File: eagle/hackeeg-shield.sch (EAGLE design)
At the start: 140 parts, among them IC1 ADS1299IPAG, IC10 TXB0108PWR, IC11 TXB0108PWR, IC2 TPS72325DBVT, IC3 TPS73225DBVT, IC5 24AA256UID, IC6 TPS60403DBVT, IC7 OPA376DBV, IC8 OPA376DBV, IC9 TXS0102DCUR

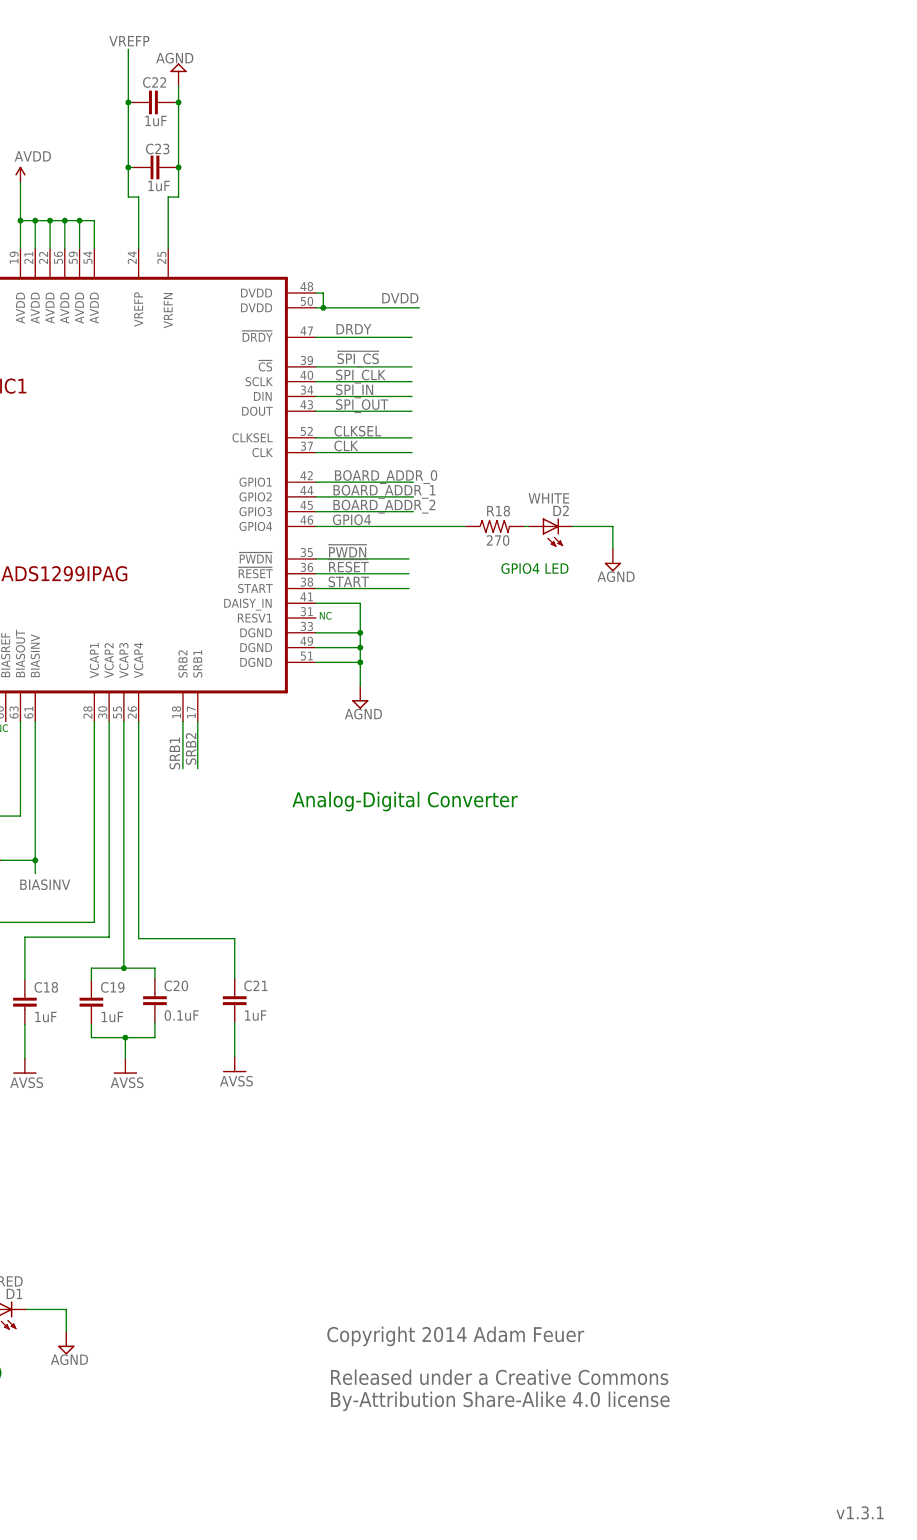
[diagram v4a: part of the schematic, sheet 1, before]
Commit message: fix for bipolar mode 2.25x problem (VREFN-AVSS)
- disconnected VREFN from AGND
- connected VREFN to AVSS
- rerouted traces
- minor labeling changes - labeled all board to board connectors
- bumped version to 1.4.0
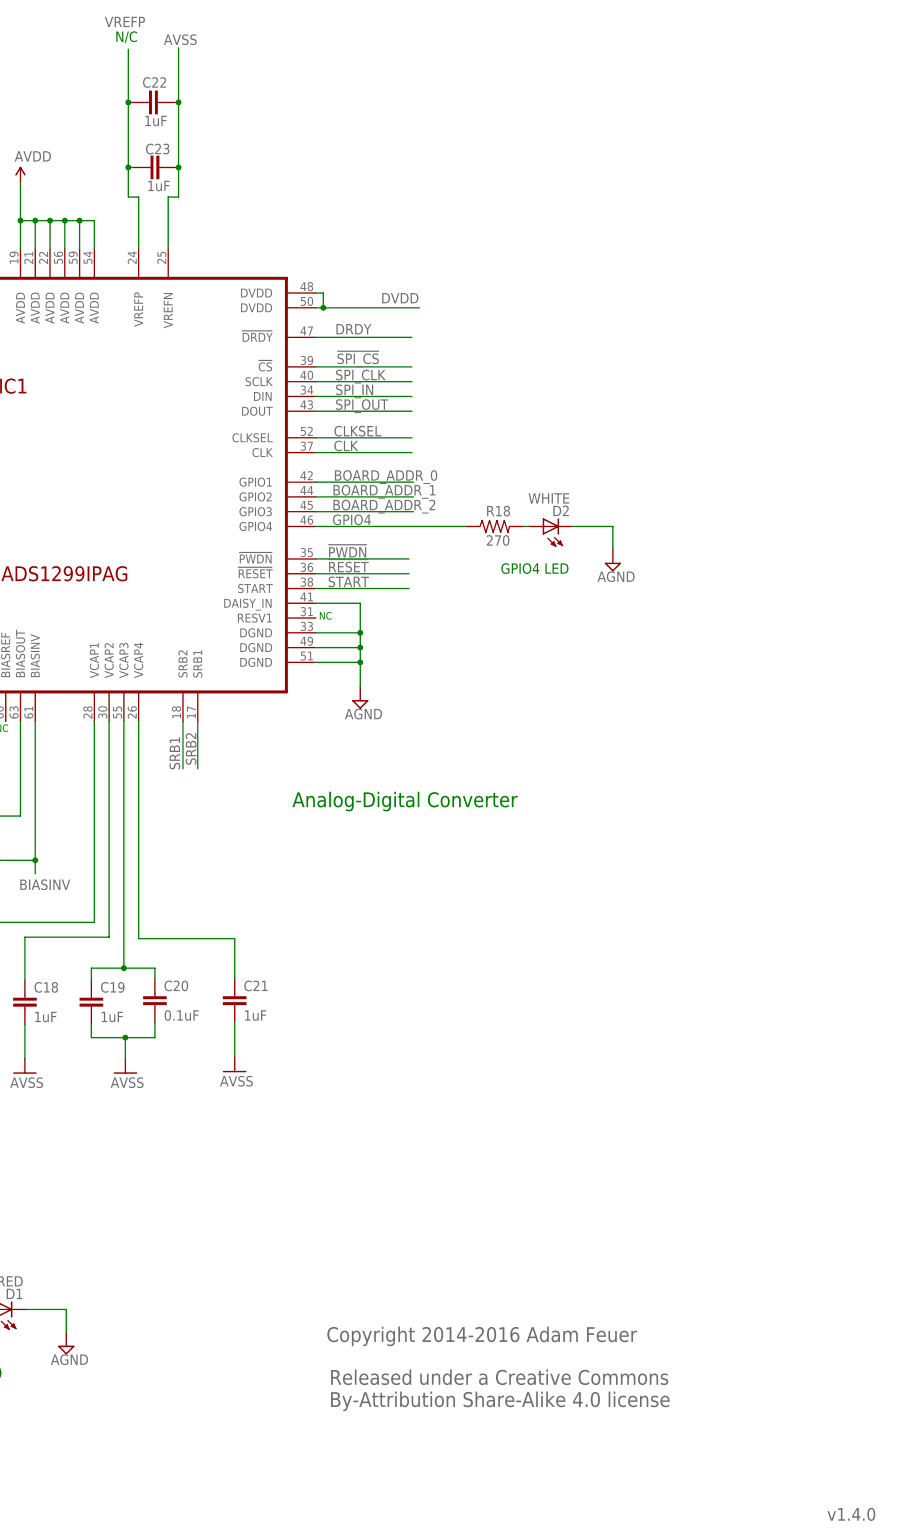
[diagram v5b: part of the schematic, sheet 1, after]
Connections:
- net AGND: no longer C22.2, C23.2, IC1.VREFN
- net AVSS: now also C22.2, C23.2, IC1.VREFN
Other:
- note added: "Copyright 2014-2016 Adam Feuer"
- note added: "N/C"
- note added: "v1.4.0"
- note removed: "Copyright 2014 Adam Feuer"
- note removed: "v1.3.1"
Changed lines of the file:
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@@
 <setting verticaltext="up"/>
 </settings>
-<grid distance="0.1" unitdist="inch" unit="inch" style="lines" multiple="1" display="no" altdistance="0.01" altunitdist="inch" altunit="inch"/>
+<grid distance="0.01" unitdist="inch" unit="inch" style="lines" multiple="1" display="no" altdistance="0.001" altunitdist="inch" altunit="inch"/>
 <layers>
 <layer number="1" name="Top" color="4" fill="1" visible="no" active="no"/>
@@
 <part name="SUPPLY10" library="supply2" deviceset="AGND" device=""/>
 <part name="SUPPLY15" library="supply2" deviceset="AGND" device=""/>
-<part name="SUPPLY20" library="supply2" deviceset="AGND" device=""/>
 <part name="AVSS1" library="SparkFun-Aesthetics" deviceset="GND" device="" value="AVSS"/>
 <part name="AVSS2" library="SparkFun-Aesthetics" deviceset="GND" device="" value="AVSS"/>
@@
 <text x="329.184" y="26.416" size="2.54" layer="95">Released under a Creative Commons
 By-Attribution Share-Alike 4.0 license</text>
-<text x="328.676" y="37.592" size="2.54" layer="95">Copyright 2014 Adam Feuer</text>
-<text x="416.306" y="7.112" size="2.1844" layer="95">v1.3.1</text>
+<text x="328.676" y="37.592" size="2.54" layer="95">Copyright 2014-2016 Adam Feuer</text>
+<text x="414.782" y="6.858" size="2.1844" layer="95">v1.4.0</text>
 <text x="246.634" y="212.344" size="1.778" layer="91">NC</text>
 <text x="327.406" y="161.798" size="1.27" layer="91">NC</text>
@@
 <text x="256.286" y="30.988" size="2.54" layer="91">Power LED</text>
 <text x="271.78" y="142.494" size="1.27" layer="91">NC</text>
+<text x="292.354" y="261.112" size="1.778" layer="91">N/C</text>
 </plain>
 <instances>
@@
 <instance part="SUPPLY10" gate="G$1" x="81.28" y="187.96"/>
 <instance part="SUPPLY15" gate="G$1" x="48.26" y="189.484"/>
-<instance part="SUPPLY20" gate="G$1" x="303.276" y="256.032" rot="R180"/>
 <instance part="AVSS1" gate="1" x="49.276" y="233.68" smashed="yes">
 <attribute name="VALUE" x="46.736" y="231.14" size="1.778" layer="96"/>
@@
 <wire x1="295.402" y1="239.522" x2="294.64" y2="239.522" width="0.1524" layer="91"/>
 <wire x1="294.64" y1="250.698" x2="294.64" y2="259.842" width="0.1524" layer="91"/>
-<label x="291.338" y="260.35" size="1.778" layer="95"/>
+<label x="290.576" y="263.652" size="1.778" layer="95"/>
 <pinref part="C23" gate="G$1" pin="1"/>
 <junction x="294.64" y="239.522"/>
@@
 <wire x1="48.26" y1="192.024" x2="48.26" y2="196.596" width="0.1524" layer="91"/>
 <pinref part="SUPPLY15" gate="G$1" pin="AGND"/>
-</segment>
-<segment>
-<wire x1="301.498" y1="225.552" x2="301.498" y2="234.442" width="0.1524" layer="91"/>
-<wire x1="301.498" y1="234.442" x2="303.276" y2="234.442" width="0.1524" layer="91"/>
-<wire x1="303.276" y1="234.442" x2="303.276" y2="239.522" width="0.1524" layer="91"/>
-<wire x1="303.276" y1="239.522" x2="303.276" y2="250.698" width="0.1524" layer="91"/>
-<wire x1="303.276" y1="250.698" x2="303.276" y2="253.492" width="0.1524" layer="91"/>
-<junction x="303.276" y="250.698"/>
-<pinref part="C23" gate="G$1" pin="2"/>
-<wire x1="303.022" y1="239.522" x2="303.276" y2="239.522" width="0.1524" layer="91"/>
-<junction x="303.276" y="239.522"/>
-<pinref part="C22" gate="G$1" pin="2"/>
-<wire x1="303.276" y1="250.698" x2="302.768" y2="250.698" width="0.1524" layer="91"/>
-<pinref part="SUPPLY20" gate="G$1" pin="AGND"/>
-<pinref part="IC1" gate="G$1" pin="VREFN"/>
 </segment>
 <segment>
@@
 <wire x1="312.928" y1="92.456" x2="312.928" y2="86.614" width="0.1524" layer="91"/>
 </segment>
+<segment>
+<wire x1="301.498" y1="225.552" x2="301.498" y2="234.442" width="0.1524" layer="91"/>
+<wire x1="301.498" y1="234.442" x2="303.276" y2="234.442" width="0.1524" layer="91"/>
+<wire x1="303.276" y1="234.442" x2="303.276" y2="239.522" width="0.1524" layer="91"/>
+<wire x1="303.276" y1="239.522" x2="303.276" y2="250.698" width="0.1524" layer="91"/>
+<wire x1="303.276" y1="250.698" x2="303.276" y2="260.096" width="0.1524" layer="91"/>
+<junction x="303.276" y="250.698"/>
+<pinref part="C23" gate="G$1" pin="2"/>
+<wire x1="303.022" y1="239.522" x2="303.276" y2="239.522" width="0.1524" layer="91"/>
+<junction x="303.276" y="239.522"/>
+<pinref part="C22" gate="G$1" pin="2"/>
+<wire x1="303.276" y1="250.698" x2="302.768" y2="250.698" width="0.1524" layer="91"/>
+<pinref part="IC1" gate="G$1" pin="VREFN"/>
+<label x="300.736" y="260.604" size="1.778" layer="95"/>
+</segment>
 </net>
 <net name="BIASINV" class="0">
@@
 <text x="320.802" y="26.416" size="2.54" layer="95">Released under a Creative Commons
 By-Attribution Share-Alike 4.0 license</text>
-<text x="320.294" y="37.592" size="2.54" layer="95">Copyright 2014 Adam Feuer</text>
+<text x="320.294" y="37.592" size="2.54" layer="95">Copyright 2014-2016 Adam Feuer</text>
 <text x="65.532" y="264.668" size="2.54" layer="91">Input Filtering</text>
 <text x="160.274" y="254.762" size="2.54" layer="91">(This side to ADS1299 inputs)</text>
@@
 <text x="326.136" y="26.416" size="2.54" layer="95">Released under a Creative Commons
 By-Attribution Share-Alike 4.0 license</text>
-<text x="325.628" y="37.592" size="2.54" layer="95">Copyright 2014 Adam Feuer</text>
+<text x="325.628" y="37.592" size="2.54" layer="95">Copyright 2014-2016 Adam Feuer</text>
 <text x="315.468" y="84.582" size="2.54" layer="91">Shield Connectors</text>
 <text x="356.616" y="254" size="1.524" layer="91">SCL1</text>

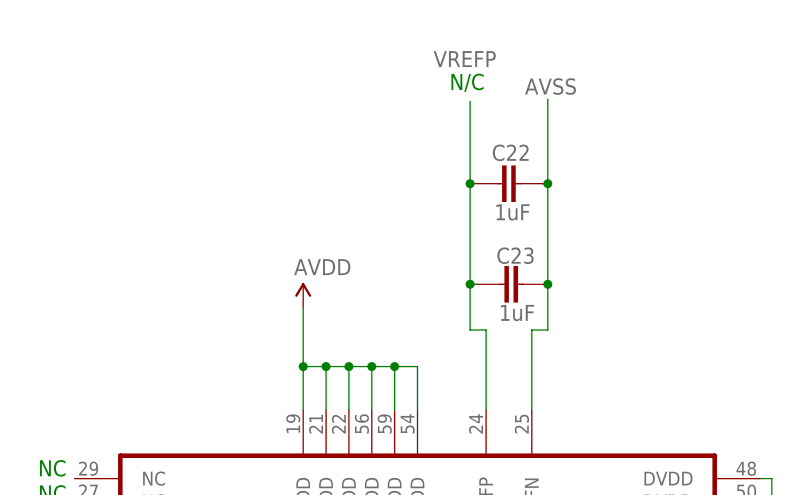
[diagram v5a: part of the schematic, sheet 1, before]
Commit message: changed C22 to 10uF; C23 to 0.1uF
- to match eval board schematic
- and added VREFP test point
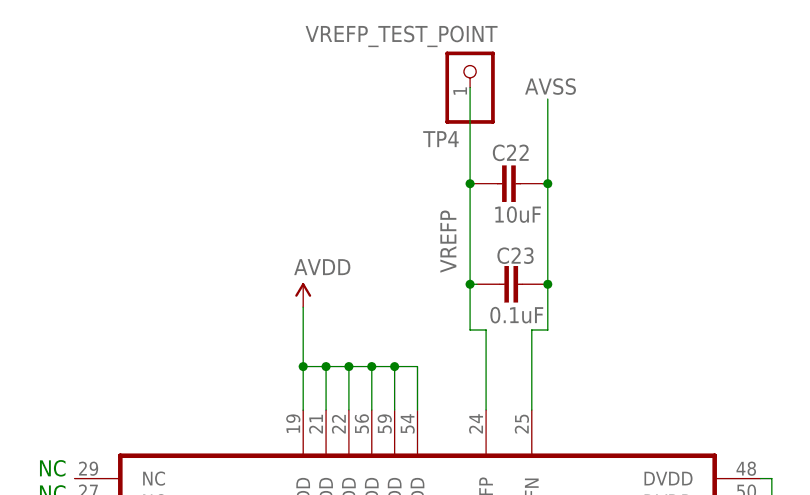
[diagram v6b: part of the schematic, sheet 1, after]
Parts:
- added TP4: VREFP_TEST_POINT, adafruit:PINHD-1X1
- C22: value 1uF -> 10uF
- C23: value 1uF -> 0.1uF
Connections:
- net VREFP: now also TP4.1
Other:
- note removed: "N/C"
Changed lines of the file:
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@@
 <setting verticaltext="up"/>
 </settings>
-<grid distance="0.01" unitdist="inch" unit="inch" style="lines" multiple="1" display="no" altdistance="0.001" altunitdist="inch" altunit="inch"/>
+<grid distance="0.1" unitdist="inch" unit="inch" style="lines" multiple="1" display="no" altdistance="0.01" altunitdist="inch" altunit="inch"/>
 <layers>
-<layer number="1" name="Top" color="4" fill="1" visible="no" active="no"/>
-<layer number="2" name="Route2" color="1" fill="3" visible="no" active="no"/>
-<layer number="3" name="Route3" color="4" fill="3" visible="no" active="no"/>
-<layer number="14" name="Route14" color="1" fill="6" visible="no" active="no"/>
-<layer number="15" name="Route15" color="4" fill="6" visible="no" active="no"/>
-<layer number="16" name="Bottom" color="1" fill="1" visible="no" active="no"/>
-<layer number="17" name="Pads" color="2" fill="1" visible="no" active="no"/>
-<layer number="18" name="Vias" color="2" fill="1" visible="no" active="no"/>
-<layer number="19" name="Unrouted" color="6" fill="1" visible="no" active="no"/>
-<layer number="20" name="Dimension" color="15" fill="1" visible="no" active="no"/>
-<layer number="21" name="tPlace" color="7" fill="1" visible="no" active="no"/>
-<layer number="22" name="bPlace" color="7" fill="1" visible="no" active="no"/>
-<layer number="23" name="tOrigins" color="15" fill="1" visible="no" active="no"/>
-<layer number="24" name="bOrigins" color="15" fill="1" visible="no" active="no"/>
-<layer number="25" name="tNames" color="7" fill="1" visible="no" active="no"/>
-<layer number="26" name="bNames" color="7" fill="1" visible="no" active="no"/>
-<layer number="27" name="tValues" color="7" fill="1" visible="no" active="no"/>
-<layer number="28" name="bValues" color="7" fill="1" visible="no" active="no"/>
+<layer number="1" name="Top" color="4" fill="1" visible="yes" active="no"/>
+<layer number="2" name="Route2" color="3" fill="1" visible="yes" active="no"/>
+<layer number="3" name="Route3" color="4" fill="3" visible="yes" active="no"/>
+<layer number="14" name="Route14" color="1" fill="6" visible="yes" active="no"/>
+<layer number="15" name="Route15" color="15" fill="1" visible="yes" active="no"/>
+<layer number="16" name="Bottom" color="1" fill="1" visible="yes" active="no"/>
+<layer number="17" name="Pads" color="2" fill="1" visible="yes" active="no"/>
+<layer number="18" name="Vias" color="2" fill="1" visible="yes" active="no"/>
+<layer number="19" name="Unrouted" color="14" fill="1" visible="yes" active="no"/>
+<layer number="20" name="Dimension" color="15" fill="1" visible="yes" active="no"/>
+<layer number="21" name="tPlace" color="7" fill="1" visible="yes" active="no"/>
+<layer number="22" name="bPlace" color="7" fill="1" visible="yes" active="no"/>
+<layer number="23" name="tOrigins" color="15" fill="1" visible="yes" active="no"/>
+<layer number="24" name="bOrigins" color="15" fill="1" visible="yes" active="no"/>
+<layer number="25" name="tNames" color="7" fill="1" visible="yes" active="no"/>
+<layer number="26" name="bNames" color="7" fill="1" visible="yes" active="no"/>
+<layer number="27" name="tValues" color="7" fill="1" visible="yes" active="no"/>
+<layer number="28" name="bValues" color="7" fill="1" visible="yes" active="no"/>
 <layer number="29" name="tStop" color="3" fill="9" visible="no" active="no"/>
 <layer number="30" name="bStop" color="7" fill="6" visible="no" active="no"/>
@@
 <layer number="35" name="tGlue" color="7" fill="4" visible="no" active="no"/>
 <layer number="36" name="bGlue" color="7" fill="5" visible="no" active="no"/>
-<layer number="37" name="tTest" color="7" fill="1" visible="no" active="no"/>
-<layer number="38" name="bTest" color="7" fill="1" visible="no" active="no"/>
+<layer number="37" name="tTest" color="7" fill="1" visible="yes" active="no"/>
+<layer number="38" name="bTest" color="7" fill="1" visible="yes" active="no"/>
 <layer number="39" name="tKeepout" color="13" fill="1" visible="no" active="no"/>
 <layer number="40" name="bKeepout" color="5" fill="1" visible="no" active="no"/>
@@
 <layer number="44" name="Drills" color="7" fill="1" visible="no" active="no"/>
 <layer number="45" name="Holes" color="7" fill="1" visible="no" active="no"/>
-<layer number="46" name="Milling" color="3" fill="1" visible="no" active="no"/>
-<layer number="47" name="Measures" color="7" fill="1" visible="no" active="no"/>
-<layer number="48" name="Document" color="7" fill="1" visible="no" active="no"/>
-<layer number="49" name="Reference" color="7" fill="1" visible="no" active="no"/>
-<layer number="50" name="dxf" color="7" fill="1" visible="no" active="no"/>
-<layer number="51" name="tDocu" color="6" fill="1" visible="no" active="no"/>
-<layer number="52" name="bDocu" color="6" fill="1" visible="no" active="no"/>
-<layer number="53" name="tGND_GNDA" color="7" fill="9" visible="no" active="no"/>
-<layer number="54" name="bGND_GNDA" color="1" fill="9" visible="no" active="no"/>
-<layer number="56" name="wert" color="7" fill="1" visible="no" active="no"/>
-<layer number="57" name="tCAD" color="7" fill="1" visible="no" active="no"/>
+<layer number="46" name="Milling" color="3" fill="1" visible="yes" active="no"/>
+<layer number="47" name="Measures" color="7" fill="1" visible="yes" active="no"/>
+<layer number="48" name="Document" color="7" fill="1" visible="yes" active="no"/>
+<layer number="49" name="Reference" color="7" fill="1" visible="yes" active="no"/>
+<layer number="50" name="dxf" color="7" fill="1" visible="yes" active="no"/>
+<layer number="51" name="tDocu" color="6" fill="1" visible="yes" active="no"/>
+<layer number="52" name="bDocu" color="6" fill="1" visible="yes" active="no"/>
+<layer number="53" name="tGND_GNDA" color="7" fill="9" visible="yes" active="no"/>
+<layer number="54" name="bGND_GNDA" color="1" fill="9" visible="yes" active="no"/>
+<layer number="56" name="wert" color="7" fill="1" visible="yes" active="no"/>
+<layer number="57" name="tCAD" color="7" fill="1" visible="yes" active="no"/>
 <layer number="91" name="Nets" color="2" fill="1" visible="yes" active="yes"/>
 <layer number="92" name="Busses" color="1" fill="1" visible="yes" active="yes"/>
@@
 <part name="C20" library="SparkFun-Passives" deviceset="CAP" device="0603-CAP" value="0.1uF"/>
 <part name="C21" library="SparkFun-Passives" deviceset="CAP" device="0603-CAP" value="1uF"/>
-<part name="C22" library="SparkFun-Passives" deviceset="CAP" device="0603-CAP" value="1uF"/>
-<part name="C23" library="SparkFun-Passives" deviceset="CAP" device="0603-CAP" value="1uF"/>
+<part name="C22" library="SparkFun-Passives" deviceset="CAP" device="0603-CAP" value="10uF"/>
+<part name="C23" library="SparkFun-Passives" deviceset="CAP" device="0603-CAP" value="0.1uF"/>
 <part name="SUPPLY2" library="supply2" deviceset="AGND" device=""/>
 <part name="SUPPLY3" library="supply2" deviceset="AGND" device=""/>
@@
 <part name="IC8" library="OPA376" deviceset="OPA376" device="DBV"/>
 <part name="IC7" library="OPA376" deviceset="OPA376" device="DBV"/>
+<part name="TP4" library="adafruit" deviceset="PINHD-1X1" device="" value="VREFP_TEST_POINT"/>
 </parts>
 <sheets>
@@
 <text x="256.286" y="30.988" size="2.54" layer="91">Power LED</text>
 <text x="271.78" y="142.494" size="1.27" layer="91">NC</text>
-<text x="292.354" y="261.112" size="1.778" layer="91">N/C</text>
 </plain>
 <instances>
@@
 <instance part="C22" gate="G$1" x="300.228" y="250.698" smashed="yes" rot="R90">
 <attribute name="NAME" x="301.371" y="255.016" size="1.778" layer="95" rot="R180"/>
-<attribute name="VALUE" x="301.371" y="248.412" size="1.778" layer="96" rot="R180"/>
+<attribute name="VALUE" x="302.641" y="248.158" size="1.778" layer="96" rot="R180"/>
 </instance>
 <instance part="C23" gate="G$1" x="300.482" y="239.522" smashed="yes" rot="R90">
 <attribute name="NAME" x="301.879" y="243.586" size="1.778" layer="95" rot="R180"/>
-<attribute name="VALUE" x="301.879" y="237.236" size="1.778" layer="96" rot="R180"/>
+<attribute name="VALUE" x="302.895" y="236.982" size="1.778" layer="96" rot="R180"/>
 </instance>
 <instance part="SUPPLY2" gate="G$1" x="139.7" y="21.844"/>
@@
 <attribute name="NAME" x="82.042" y="48.006" size="1.778" layer="95"/>
 <attribute name="VALUE" x="82.042" y="29.972" size="1.27" layer="96"/>
+</instance>
+<instance part="TP4" gate="G$1" x="294.64" y="263.906" smashed="yes" rot="MR90">
+<attribute name="NAME" x="293.497" y="254.762" size="1.778" layer="95" rot="MR0"/>
+<attribute name="VALUE" x="297.688" y="266.446" size="1.778" layer="96" rot="MR0"/>
 </instance>
 </instances>
@@
 <pinref part="C22" gate="G$1" pin="1"/>
 <wire x1="295.402" y1="239.522" x2="294.64" y2="239.522" width="0.1524" layer="91"/>
-<wire x1="294.64" y1="250.698" x2="294.64" y2="259.842" width="0.1524" layer="91"/>
-<label x="290.576" y="263.652" size="1.778" layer="95"/>
+<wire x1="294.64" y1="250.698" x2="294.64" y2="261.366" width="0.1524" layer="91"/>
+<label x="293.116" y="240.792" size="1.778" layer="95" rot="R90"/>
 <pinref part="C23" gate="G$1" pin="1"/>
 <junction x="294.64" y="239.522"/>
 <junction x="294.64" y="250.698"/>
 <pinref part="IC1" gate="G$1" pin="VREFP"/>
-</segment>
-</net>
+<pinref part="TP4" gate="G$1" pin="1"/>
+</segment>
+</net>
